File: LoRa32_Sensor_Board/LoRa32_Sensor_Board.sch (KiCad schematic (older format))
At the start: 19 parts, among them J1 Battery holder, U1 LSM303C, U2 TTGO_LoRa32, U3 MPL115A1, U4 ublox_SAM-M8Q, U5 STC3100

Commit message: PCB finished
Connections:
- net MOSI: now reaches U2.14 (MOSI), U3.7 (DIN)
- net MPL115A1_SHDN: now reaches R1.1, U2.20 (IO17), U3.4 (~SHDN)
- net SCK: now reaches U2.24 (SCK), U3.8 (SCLK)
- net MISO: now reaches U2.27 (MISO), U3.6 (DOUT)
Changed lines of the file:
@@
 Wire Wire Line
 	7350 2900 7750 2900
+Text Label 5950 3350 0    50   ~ 0
+SCK
+Text Label 5950 3450 0    50   ~ 0
+MOSI
+Text Label 5950 3550 0    50   ~ 0
+MISO
+Text Label 5900 3750 0    50   ~ 0
+MPL115A1_SHDN
 $EndSCHEMATC

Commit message: README.md for the hardware part added, sense resistor tracks widened
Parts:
- U1: footprint Package_LGA:LGA-12_2x2mm_P0.5mm -> LoRa32_Sensor_Board:LGA-12_2x2mm_P0.5mm_smallerpads
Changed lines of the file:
@@
 F 0 "U1" H 3850 6500 50  0000 C CNN
 F 1 "LSM303C" H 4750 5500 50  0000 C CNN
-F 2 "Package_LGA:LGA-12_2x2mm_P0.5mm" H 3950 5300 50  0001 L CNN
+F 2 "LoRa32_Sensor_Board:LGA-12_2x2mm_P0.5mm_smallerpads" H 3950 5300 50  0001 L CNN
 F 3 "www.st.com/resource/en/datasheet/lsm303c.pdf" H 4450 5350 50  0001 C CNN
 	1    4350 6000

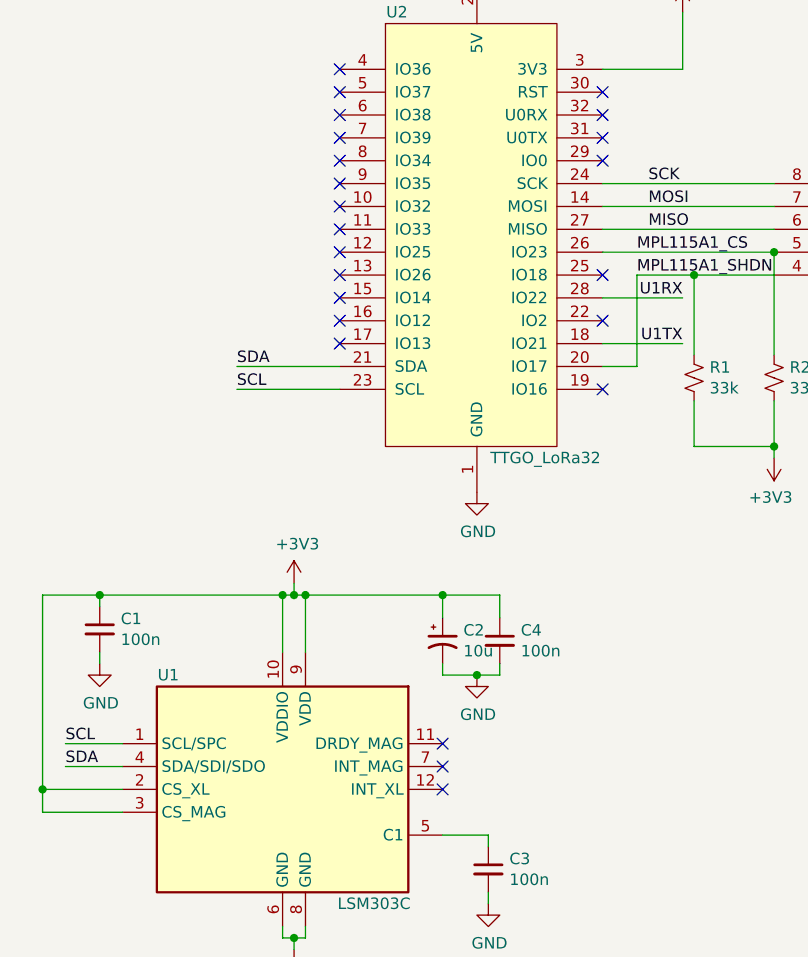
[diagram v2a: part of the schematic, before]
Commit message: DRDY_MAG, INT_XL and INT_MAG pins from LSM303C connected to ESP32
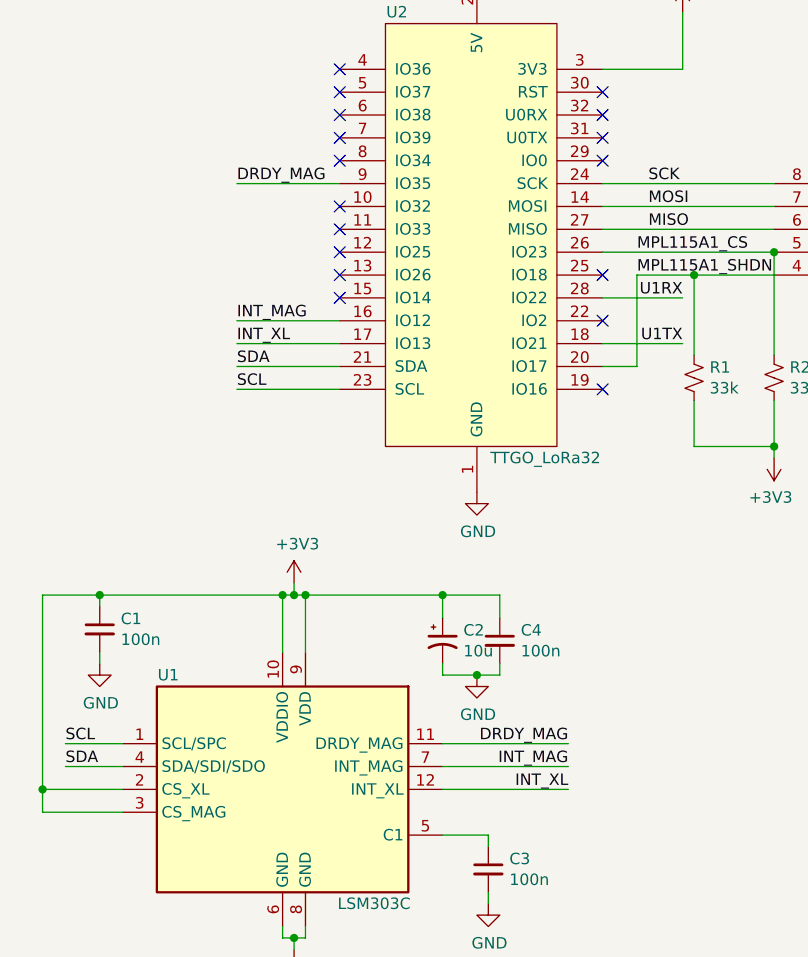
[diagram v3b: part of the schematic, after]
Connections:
- net INT_MAG: now reaches U2.16 (IO12)
- net INT_MAG: now also U1.7 (INT_MAG)
- net INT_XL: now reaches U2.17 (IO13)
- net INT_XL: now also U1.12 (INT_XL)
- net DRDY_MAG: now reaches U2.9 (IO35)
- net DRDY_MAG: now also U1.11 (DRDY_MAG)
- no-connect marks 30 -> 24
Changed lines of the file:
@@
 NoConn ~ 4600 3150
 NoConn ~ 4600 3250
-NoConn ~ 4600 3350
 NoConn ~ 4600 3450
 NoConn ~ 4600 3550
@@
 NoConn ~ 4600 3750
 NoConn ~ 4600 3850
-NoConn ~ 4600 3950
 NoConn ~ 5750 4250
 NoConn ~ 5750 3950
@@
 	1    0    0    -1
 $EndComp
-NoConn ~ 5050 5800
-NoConn ~ 5050 5900
-NoConn ~ 5050 6000
 Wire Wire Line
 	6100 2600 6100 2850
-$Comp
-L ttgo_lora32:TTGO_LoRa32 U2
-U 1 1 5CA16B34
-P 5200 3550
-F 0 "U2" H 4850 4500 50  0000 C CNN
-F 1 "TTGO_LoRa32" H 5500 2550 50  0000 C CNN
-F 2 "LoRa32_Sensor_Board:TTGO_LoRa32" H 4600 4250 50  0001 C CNN
-F 3 "" H 4600 4250 50  0001 C CNN
-	1    5200 3550
-	1    0    0    -1
-$EndComp
-NoConn ~ 4600 4050
 NoConn ~ 5750 2950
 NoConn ~ 5750 3050
@@
 Text Label 5900 3750 0    50   ~ 0
 MPL115A1_SHDN
+$Comp
+L ttgo_lora32:TTGO_LoRa32 U2
+U 1 1 5CA16B34
+P 5200 3550
+F 0 "U2" H 4850 4500 50  0000 C CNN
+F 1 "TTGO_LoRa32" H 5500 2550 50  0000 C CNN
+F 2 "LoRa32_Sensor_Board:TTGO_LoRa32" H 4600 4250 50  0001 C CNN
+F 3 "" H 4600 4250 50  0001 C CNN
+	1    5200 3550
+	1    0    0    -1
+$EndComp
+Text Label 5600 5800 2    50   ~ 0
+DRDY_MAG
+Text Label 5600 5900 2    50   ~ 0
+INT_MAG
+Text Label 5600 6000 2    50   ~ 0
+INT_XL
+Wire Wire Line
+	5600 5800 5050 5800
+Wire Wire Line
+	5050 5900 5600 5900
+Wire Wire Line
+	5600 6000 5050 6000
+Text Label 4150 3350 0    50   ~ 0
+DRDY_MAG
+Text Label 4150 3950 0    50   ~ 0
+INT_MAG
+Text Label 4150 4050 0    50   ~ 0
+INT_XL
+Wire Wire Line
+	4150 3350 4600 3350
+Wire Wire Line
+	4150 4050 4600 4050
+Wire Wire Line
+	4150 3950 4600 3950
 $EndSCHEMATC
